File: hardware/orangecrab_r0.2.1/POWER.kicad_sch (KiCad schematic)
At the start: 43 parts, among them J5 JST, U1 TLV62569DRL, U10 NCP115-2.5, U2 TLV62569DRL, U5 BQ24232, U7 TLV62569DRL

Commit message: all IO gone/cleaned
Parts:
- removed C12, C13, C77: 4.7uF, Capacitor_SMD:C_0402_1005Metric, symbol Device:C
- removed D2: LED_ARGB, gkl_led:0404LED_RGB, symbol Device:LED_ARGB
- removed J5: JST, gkl_conn:JST_PH_B2B-PH-SM4-TB_1x02-1MP_P2.00mm_Vertical, symbol Connector_Generic_MountingPin:Conn_01x02_MountingPin
- removed R10: 56.2k, gkl_dipol:R_0201_0603Metric, symbol Device:R
- removed R11: 3.09k, gkl_dipol:R_0201_0603Metric, symbol Device:R
- removed R12: 4.32k, gkl_dipol:R_0201_0603Metric, symbol Device:R
- removed R26, R7: 10k, gkl_dipol:R_0201_0603Metric, symbol Device:R
- removed R8: 4.7k, gkl_dipol:R_0201_0603Metric, symbol Device:R
- removed R9: 3.57k, gkl_dipol:R_0201_0603Metric, symbol Device:R
- removed U5: BQ24232, Package_DFN_QFN:QFN-16-1EP_3x3mm_P0.5mm_EP1.75x1.75mm, symbol gkl_pmic:BQ24230
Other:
- note removed: "Battery Charger"
- note removed: "Battery Input"
- note removed: "Charge Current Set by ILIM"
- note removed: "D2: Green: USB present Yellow: battery is charging"

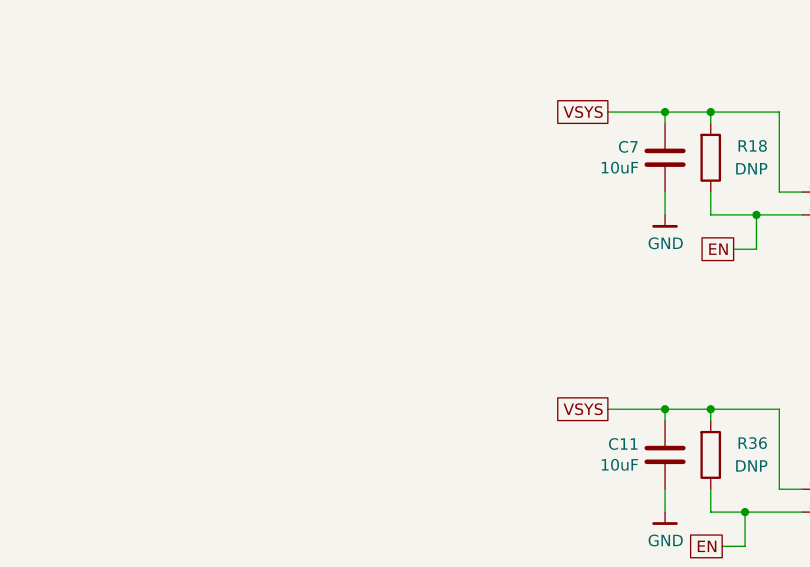
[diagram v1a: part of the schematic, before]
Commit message: delete redundant sheets
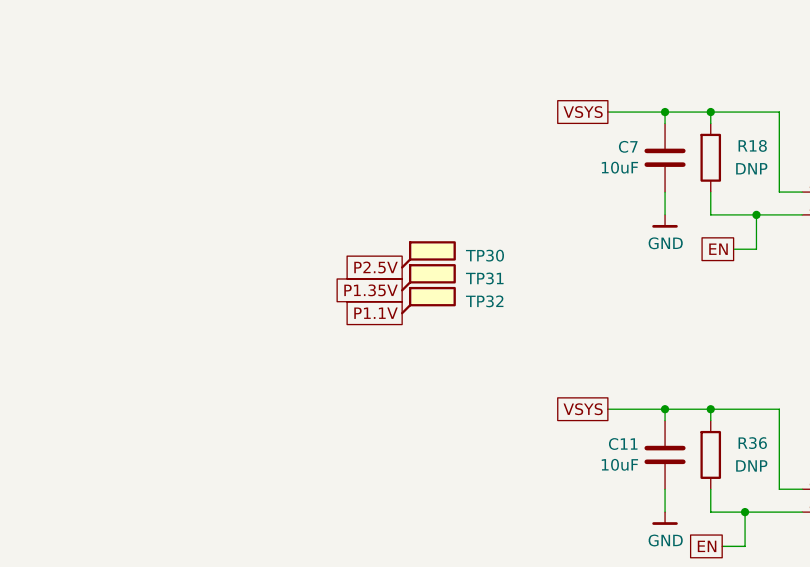
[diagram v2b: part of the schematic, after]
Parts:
- added TP30, TP31, TP32: SMD_TP, gkl_misc:TestPoint_Pad_D0.5mm, symbol Connector:TestPoint_Flag
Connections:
- net P1.1V: now also TP32.1
- net P1.35V: now also TP31.1
- net P2.5V: now also TP30.1
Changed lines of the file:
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@@
+    )
+  )
+  (global_label "P1.35V" (shape passive) (at 152.4 103.632 180)
+    (effects (font (size 1.27 1.27)) (justify right))
+    (property "Intersheetrefs" "${INTERSHEET_REFS}" (at 152.4 103.632 0)
+      (effects (font (size 1.27 1.27)) hide)
+    )
+  )
+  (global_label "P1.1V" (shape passive) (at 152.4 106.172 180)
+    (effects (font (size 1.27 1.27)) (justify right))
+    (property "Intersheetrefs" "${INTERSHEET_REFS}" (at 152.4 106.172 0)
+      (effects (font (size 1.27 1.27)) hide)
     )
   )
@@
     (effects (font (size 1.27 1.27)) (justify left))
     (property "Intersheetrefs" "${INTERSHEET_REFS}" (at 252.73 48.26 0)
+      (effects (font (size 1.27 1.27)) hide)
+    )
+  )
+  (global_label "P2.5V" (shape passive) (at 152.4 101.092 180)
+    (effects (font (size 1.27 1.27)) (justify right))
+    (property "Intersheetrefs" "${INTERSHEET_REFS}" (at 152.4 101.092 0)
       (effects (font (size 1.27 1.27)) hide)
     )
@@
         )
       )
+    )
+  )
+  (symbol (lib_id "Connector:TestPoint_Flag") (at 152.4 106.172 0) (unit 1)
+    (in_bom yes) (on_board yes) (dnp no)
+    (property "Reference" "TP32" (at 163.83 104.902 0)
+      (effects (font (size 1.27 1.27)) (justify right))
+    )
+    (property "Value" "SMD_TP" (at 151.2824 106.0958 0)
+      (effects (font (size 1.27 1.27)) (justify right) hide)
+    )
+    (property "Footprint" "gkl_misc:TestPoint_Pad_D0.5mm" (at 157.48 106.172 0)
+      (effects (font (size 1.27 1.27)) hide)
+    )
+    (property "Datasheet" "~" (at 157.48 106.172 0)
+      (effects (font (size 1.27 1.27)) hide)
+    )
+    (property "PN" "DNP" (at 152.4 106.172 0)
+      (effects (font (size 1.27 1.27)) hide)
+    )
+    (pin "1")
+    (instances
+      (project "OrangeCrab"
+        (path "/3fc0bb0e-dabc-4b81-bef6-ad7dd3f01477/00000000-0000-0000-0000-00005d1738db"
+          (reference "TP32") (unit 1)
+        )
+      )
+    )
+  )
+  (symbol (lib_id "Connector:TestPoint_Flag") (at 152.4 103.632 0) (unit 1)
+    (in_bom yes) (on_board yes) (dnp no)
+    (property "Reference" "TP31" (at 163.83 102.362 0)
+      (effects (font (size 1.27 1.27)) (justify right))
+    )
+    (property "Value" "SMD_TP" (at 151.2824 103.5558 0)
+      (effects (font (size 1.27 1.27)) (justify right) hide)
+    )
+    (property "Footprint" "gkl_misc:TestPoint_Pad_D0.5mm" (at 157.48 103.632 0)
+      (effects (font (size 1.27 1.27)) hide)
+    )
+    (property "Datasheet" "~" (at 157.48 103.632 0)
+      (effects (font (size 1.27 1.27)) hide)
+    )
+    (property "PN" "DNP" (at 152.4 103.632 0)
+      (effects (font (size 1.27 1.27)) hide)
+    )
+    (pin "1")
+    (instances
+      (project "OrangeCrab"
+        (path "/3fc0bb0e-dabc-4b81-bef6-ad7dd3f01477/00000000-0000-0000-0000-00005d1738db"
+          (reference "TP31") (unit 1)
+        )
+      )
+    )
+  )
+  (symbol (lib_id "Connector:TestPoint_Flag") (at 152.4 101.092 0) (unit 1)
+    (in_bom yes) (on_board yes) (dnp no)
+    (property "Reference" "TP30" (at 163.83 99.822 0)
+      (effects (font (size 1.27 1.27)) (justify right))
+    )
+    (property "Value" "SMD_TP" (at 151.2824 101.0158 0)
+      (effects (font (size 1.27 1.27)) (justify right) hide)
+    )
+    (property "Footprint" "gkl_misc:TestPoint_Pad_D0.5mm" (at 157.48 101.092 0)
+      (effects (font (size 1.27 1.27)) hide)
+    )
+    (property "Datasheet" "~" (at 157.48 101.092 0)
+      (effects (font (size 1.27 1.27)) hide)
+    )
+    (property "PN" "DNP" (at 152.4 101.092 0)
+      (effects (font (size 1.27 1.27)) hide)
+    )
+    (pin "1")
+    (instances
+      (project "OrangeCrab"
+        (path "/3fc0bb0e-dabc-4b81-bef6-ad7dd3f01477/00000000-0000-0000-0000-00005d1738db"
+          (reference "TP30") (unit 1)
+        )
+      )

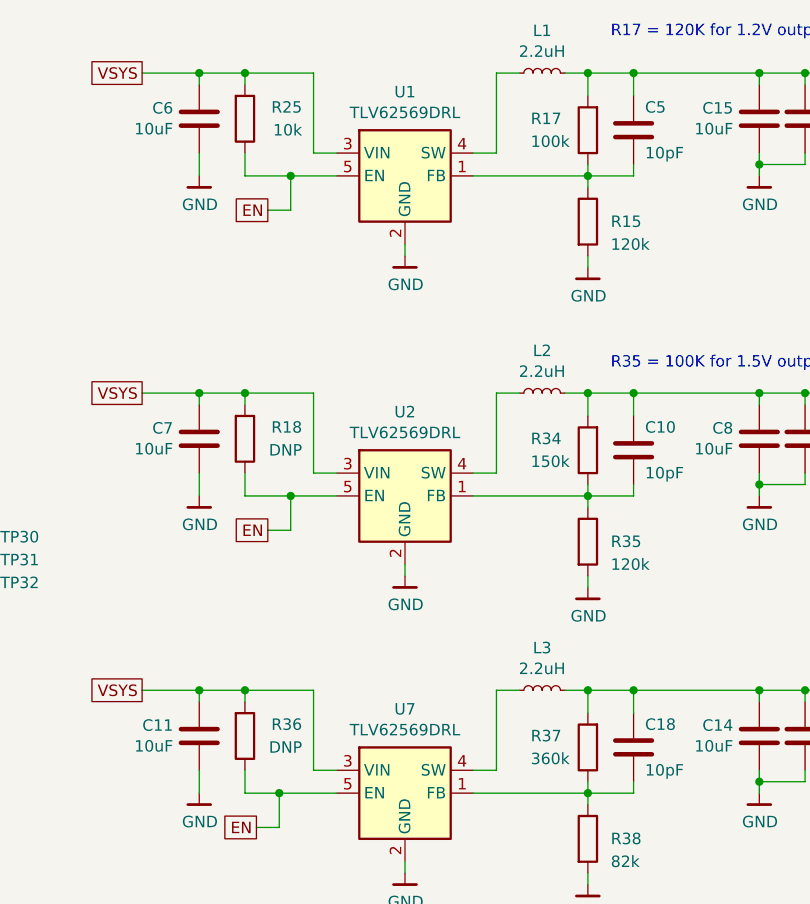
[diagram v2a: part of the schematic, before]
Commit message: add some LCSC part numbers, stock all important parts
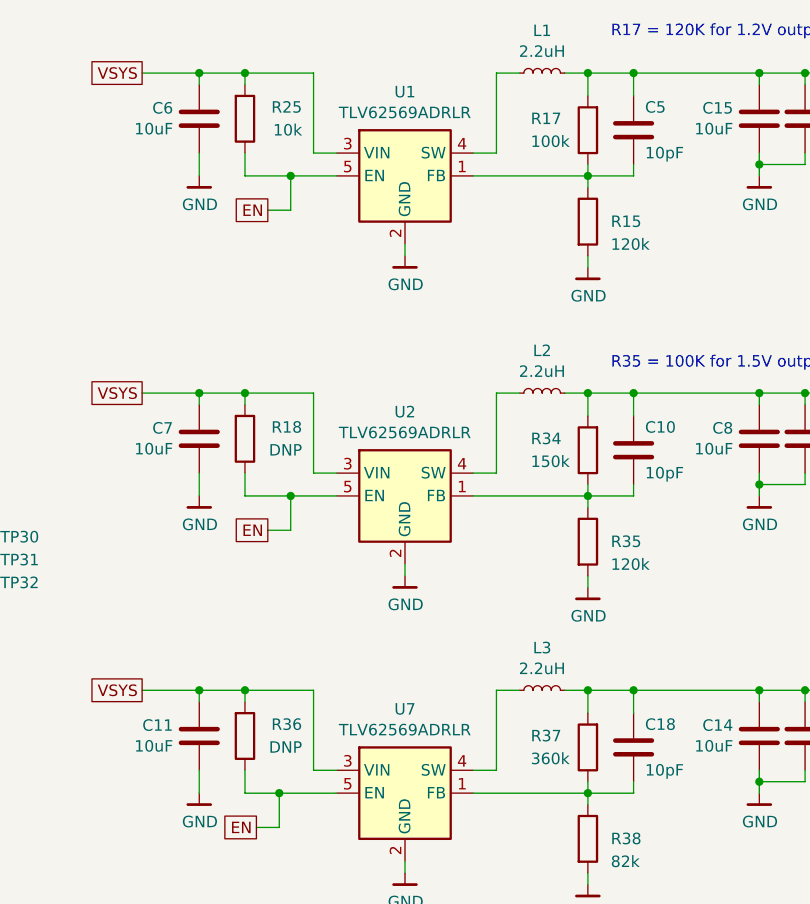
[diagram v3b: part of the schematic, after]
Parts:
- C10, C18, C5: lcsc# (none) -> C526922
- C11, C14, C15, C16, C17, C6, C7, C8, C9: lcsc# (none) -> C105884
- C46, C47: lcsc# (none) -> C326586
- L1, L2, L3: lcsc# (none) -> C216156
- U1, U2, U7: value TLV62569DRL -> TLV62569ADRLR; lcsc# (none) -> C398367
- U10: PN NCP115CMX250TCG -> NCP115AMX250TCG
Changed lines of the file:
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@@
+      (effects (font (size 1.27 1.27)) hide)
+    )
+    (property "lcsc#" "C216156" (at 219.71 48.26 0)
       (effects (font (size 1.27 1.27)) hide)
     )
@@
       (effects (font (size 1.27 1.27)) hide)
     )
+    (property "lcsc#" "" (at 224.79 64.77 0)
+      (effects (font (size 1.27 1.27)) hide)
+    )
     (pin "1")
     (pin "2")
@@
       (effects (font (size 1.27 1.27)) hide)
     )
+    (property "lcsc#" "" (at 224.79 54.61 0)
+      (effects (font (size 1.27 1.27)) hide)
+    )
     (pin "1")
     (pin "2")
@@
       (effects (font (size 1.27 1.27)) hide)
     )
+    (property "lcsc#" "C105884" (at 243.84 53.34 0)
+      (effects (font (size 1.27 1.27)) hide)
+    )
     (pin "1")
     (pin "2")
@@
       (effects (font (size 1.27 1.27)) hide)
     )
+    (property "lcsc#" "C105884" (at 248.92 53.34 0)
+      (effects (font (size 1.27 1.27)) hide)
+    )
     (pin "1")
     (pin "2")
@@
       (effects (font (size 1.27 1.27)) hide)
     )
+    (property "lcsc#" "C526922" (at 229.87 54.61 0)
+      (effects (font (size 1.27 1.27)) hide)
+    )
     (pin "1")
     (pin "2")
@@
       (effects (font (size 1.27 1.27)) hide)
     )
-    (property "PN" "NCP115CMX250TCG" (at 93.98 152.4 0)
+    (property "PN" "NCP115AMX250TCG" (at 93.98 152.4 0)
       (effects (font (size 1.27 1.27)) hide)
     )
     (property "Mfg" "ON Semiconductor" (at 93.98 152.4 0)
+      (effects (font (size 1.27 1.27)) hide)
+    )
+    (property "lcsc#" "" (at 93.98 152.4 0)
       (effects (font (size 1.27 1.27)) hide)
     )
@@
       (effects (font (size 1.27 1.27)) hide)
     )
+    (property "lcsc#" "C326586" (at 64.77 154.94 0)
+      (effects (font (size 1.27 1.27)) hide)
+    )
     (pin "1")
     (pin "2")
@@
       (effects (font (size 1.27 1.27)) hide)
     )
+    (property "lcsc#" "C326586" (at 113.03 154.94 0)
+      (effects (font (size 1.27 1.27)) hide)
+    )
     (pin "1")
     (pin "2")
@@
       (effects (font (size 1.27 1.27)) hide)
     )
+    (property "lcsc#" "" (at 186.69 53.34 0)
+      (effects (font (size 1.27 1.27)) hide)
+    )
     (pin "1")
     (pin "2")
@@
       (effects (font (size 1.27 1.27)))
     )
-    (property "Value" "TLV62569DRL" (at 204.47 52.6796 0)
+    (property "Value" "TLV62569ADRLR" (at 204.47 52.6796 0)
       (effects (font (size 1.27 1.27)))
     )
@@
     )
     (property "PN" "TLV62569DRLR" (at 204.47 59.69 0)
+      (effects (font (size 1.27 1.27)) hide)
+    )
+    (property "lcsc#" "C398367" (at 204.47 59.69 0)
       (effects (font (size 1.27 1.27)) hide)
     )
@@
       (effects (font (size 1.27 1.27)) hide)
     )
+    (property "lcsc#" "C216156" (at 219.71 83.82 0)
+      (effects (font (size 1.27 1.27)) hide)
+    )
     (pin "1")
     (pin "2")
@@
       (effects (font (size 1.27 1.27)) hide)
     )
+    (property "lcsc#" "" (at 224.79 100.33 0)
+      (effects (font (size 1.27 1.27)) hide)
+    )
     (pin "1")
     (pin "2")
@@
       (effects (font (size 1.27 1.27)) hide)
     )
+    (property "lcsc#" "" (at 224.79 90.17 0)
+      (effects (font (size 1.27 1.27)) hide)
+    )
     (pin "1")
     (pin "2")
@@
       (effects (font (size 1.27 1.27)) hide)
     )
+    (property "lcsc#" "C105884" (at 243.84 88.9 0)
+      (effects (font (size 1.27 1.27)) hide)
+    )
     (pin "1")
     (pin "2")
@@
       (effects (font (size 1.27 1.27)) hide)
     )
+    (property "lcsc#" "C105884" (at 248.92 88.9 0)
+      (effects (font (size 1.27 1.27)) hide)
+    )
     (pin "1")
     (pin "2")
@@
       (effects (font (size 1.27 1.27)) hide)
     )
+    (property "lcsc#" "C526922" (at 229.87 90.17 0)
+      (effects (font (size 1.27 1.27)) hide)
+    )
     (pin "1")
     (pin "2")
@@
       (effects (font (size 1.27 1.27)) hide)
     )
+    (property "lcsc#" "" (at 186.69 88.9 0)
+      (effects (font (size 1.27 1.27)) hide)
+    )
     (pin "1")
     (pin "2")
@@
       (effects (font (size 1.27 1.27)))
     )
-    (property "Value" "TLV62569DRL" (at 204.47 88.2396 0)
+    (property "Value" "TLV62569ADRLR" (at 204.47 88.2396 0)
       (effects (font (size 1.27 1.27)))
     )
@@
     )
     (property "PN" "TLV62569DRLR" (at 204.47 95.25 0)
+      (effects (font (size 1.27 1.27)) hide)
+    )
+    (property "lcsc#" "C398367" (at 204.47 95.25 0)
       (effects (font (size 1.27 1.27)) hide)
     )
@@
       (effects (font (size 1.27 1.27)) hide)
     )
+    (property "lcsc#" "C216156" (at 219.71 116.84 0)
+      (effects (font (size 1.27 1.27)) hide)
+    )
     (pin "1")
     (pin "2")
@@
       (effects (font (size 1.27 1.27)) hide)
     )
+    (property "lcsc#" "" (at 224.79 133.35 0)
+      (effects (font (size 1.27 1.27)) hide)
+    )
     (pin "1")
     (pin "2")
@@
       (effects (font (size 1.27 1.27)) hide)
     )
+    (property "lcsc#" "" (at 224.79 123.19 0)
+      (effects (font (size 1.27 1.27)) hide)
+    )
     (pin "1")
     (pin "2")
@@
       (effects (font (size 1.27 1.27)) hide)
     )
+    (property "lcsc#" "C105884" (at 243.84 121.92 0)
+      (effects (font (size 1.27 1.27)) hide)
+    )
     (pin "1")
     (pin "2")
@@
       (effects (font (size 1.27 1.27)) hide)
     )
+    (property "lcsc#" "C105884" (at 248.92 121.92 0)
+      (effects (font (size 1.27 1.27)) hide)
+    )
     (pin "1")
     (pin "2")
@@
       (effects (font (size 1.27 1.27)) hide)
     )
+    (property "lcsc#" "C526922" (at 229.87 123.19 0)
+      (effects (font (size 1.27 1.27)) hide)
+    )
     (pin "1")
     (pin "2")
@@
       (effects (font (size 1.27 1.27)) hide)
     )
+    (property "lcsc#" "" (at 186.69 121.92 0)
+      (effects (font (size 1.27 1.27)) hide)
+    )
     (pin "1")
     (pin "2")
@@
       (effects (font (size 1.27 1.27)))
     )
-    (property "Value" "TLV62569DRL" (at 204.47 121.2596 0)
+    (property "Value" "TLV62569ADRLR" (at 204.47 121.2596 0)
       (effects (font (size 1.27 1.27)))
     )
@@
     )
     (property "PN" "TLV62569DRLR" (at 204.47 128.27 0)
+      (effects (font (size 1.27 1.27)) hide)
+    )
+    (property "lcsc#" "C398367" (at 204.47 128.27 0)
       (effects (font (size 1.27 1.27)) hide)
     )
@@
       (effects (font (size 1.27 1.27)) hide)
     )
+    (property "lcsc#" "C105884" (at 181.61 121.92 0)
+      (effects (font (size 1.27 1.27)) hide)
+    )
     (pin "1")
     (pin "2")
@@
       (effects (font (size 1.27 1.27)) hide)
     )
+    (property "lcsc#" "C105884" (at 181.61 88.9 0)
+      (effects (font (size 1.27 1.27)) hide)
+    )
     (pin "1")
     (pin "2")
@@
     )
     (property "PN_1" "CC0402MRX5R5BB106" (at 181.61 53.34 0)
+      (effects (font (size 1.27 1.27)) hide)
+    )
+    (property "lcsc#" "C105884" (at 181.61 53.34 0)
       (effects (font (size 1.27 1.27)) hide)
     )
@@
       (effects (font (size 1.27 1.27)) hide)
     )
+    (property "lcsc#" "" (at 152.4 106.172 0)
+      (effects (font (size 1.27 1.27)) hide)
+    )
     (pin "1")
     (instances
@@
       (effects (font (size 1.27 1.27)) hide)
     )
+    (property "lcsc#" "" (at 152.4 103.632 0)
+      (effects (font (size 1.27 1.27)) hide)
+    )
     (pin "1")
     (instances
@@
       (effects (font (size 1.27 1.27)) hide)
     )
+    (property "lcsc#" "" (at 152.4 101.092 0)
+      (effects (font (size 1.27 1.27)) hide)
+    )

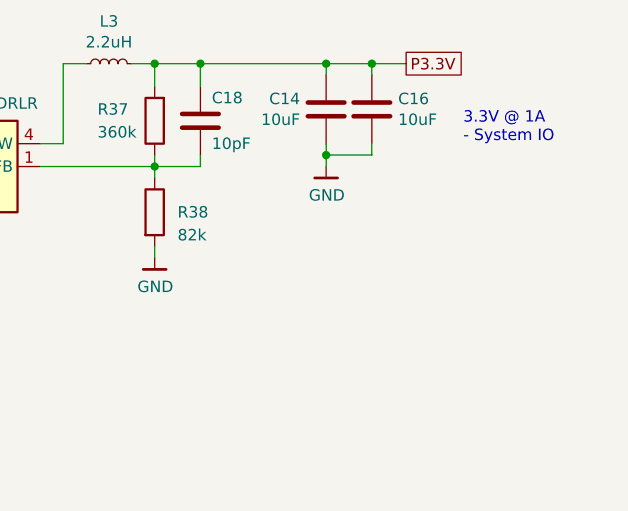
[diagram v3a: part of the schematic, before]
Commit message: populate LCSC# for missing passives
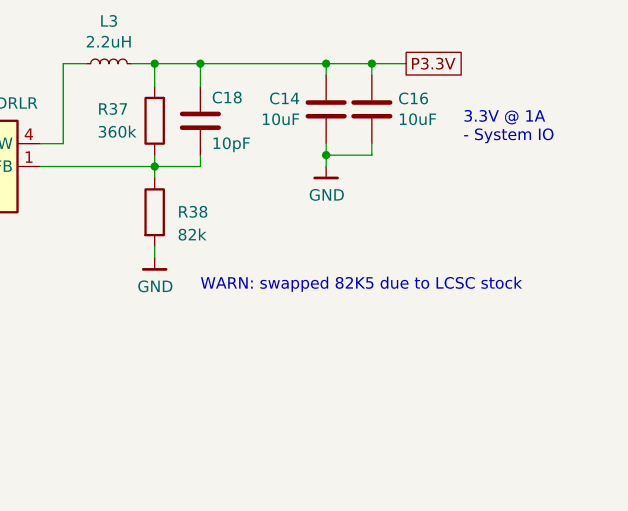
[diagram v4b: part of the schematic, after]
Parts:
- R15, R35: lcsc# (none) -> C274344
- R17: lcsc# (none) -> C106224
- R25: lcsc# (none) -> C106225
- R34: lcsc# (none) -> C274346
- R37: lcsc# (none) -> C295795
- R38: lcsc# (none) -> C327380
- U10: lcsc# (none) -> C000000
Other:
- note added: "WARN: swapped 82K5 due to LCSC stock"
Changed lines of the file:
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@@
+    (effects (font (size 1.27 1.27)) (justify left bottom))
+  )
+  (text "WARN: swapped 82K5 due to LCSC stock" (at 229.87 142.24 0)
     (effects (font (size 1.27 1.27)) (justify left bottom))
   )
@@
       (effects (font (size 1.27 1.27)) hide)
     )
-    (property "lcsc#" "" (at 224.79 64.77 0)
+    (property "lcsc#" "C274344" (at 224.79 64.77 0)
       (effects (font (size 1.27 1.27)) hide)
     )
@@
       (effects (font (size 1.27 1.27)) hide)
     )
-    (property "lcsc#" "" (at 224.79 54.61 0)
+    (property "lcsc#" "C106224" (at 224.79 54.61 0)
       (effects (font (size 1.27 1.27)) hide)
     )
@@
       (effects (font (size 1.27 1.27)) hide)
     )
-    (property "lcsc#" "" (at 93.98 152.4 0)
+    (property "lcsc#" "C000000" (at 93.98 152.4 0)
       (effects (font (size 1.27 1.27)) hide)
     )
@@
       (effects (font (size 1.27 1.27)) hide)
     )
-    (property "lcsc#" "" (at 186.69 53.34 0)
+    (property "lcsc#" "C106225" (at 186.69 53.34 0)
       (effects (font (size 1.27 1.27)) hide)
     )
@@
       (effects (font (size 1.27 1.27)) hide)
     )
-    (property "lcsc#" "" (at 224.79 100.33 0)
+    (property "lcsc#" "C274344" (at 224.79 100.33 0)
       (effects (font (size 1.27 1.27)) hide)
     )
@@
       (effects (font (size 1.27 1.27)) hide)
     )
-    (property "lcsc#" "" (at 224.79 90.17 0)
+    (property "lcsc#" "C274346" (at 224.79 90.17 0)
       (effects (font (size 1.27 1.27)) hide)
     )
@@
       (effects (font (size 1.27 1.27)) hide)
     )
-    (property "lcsc#" "" (at 224.79 133.35 0)
+    (property "lcsc#" "C327380" (at 224.79 133.35 0)
       (effects (font (size 1.27 1.27)) hide)
     )
@@
       (effects (font (size 1.27 1.27)) hide)
     )
-    (property "lcsc#" "" (at 224.79 123.19 0)
-      (effects (font (size 1.27 1.27)) hide)
-    )
+    (property "lcsc#" "C295795" (at 224.79 123.19 0)
+      (effects (font (size 1.27 1.27)) hide)
+    )
